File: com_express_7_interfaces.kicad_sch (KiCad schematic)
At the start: 1 part, among them J1 Plug_Bus_CE7_EPT_401-55501-51

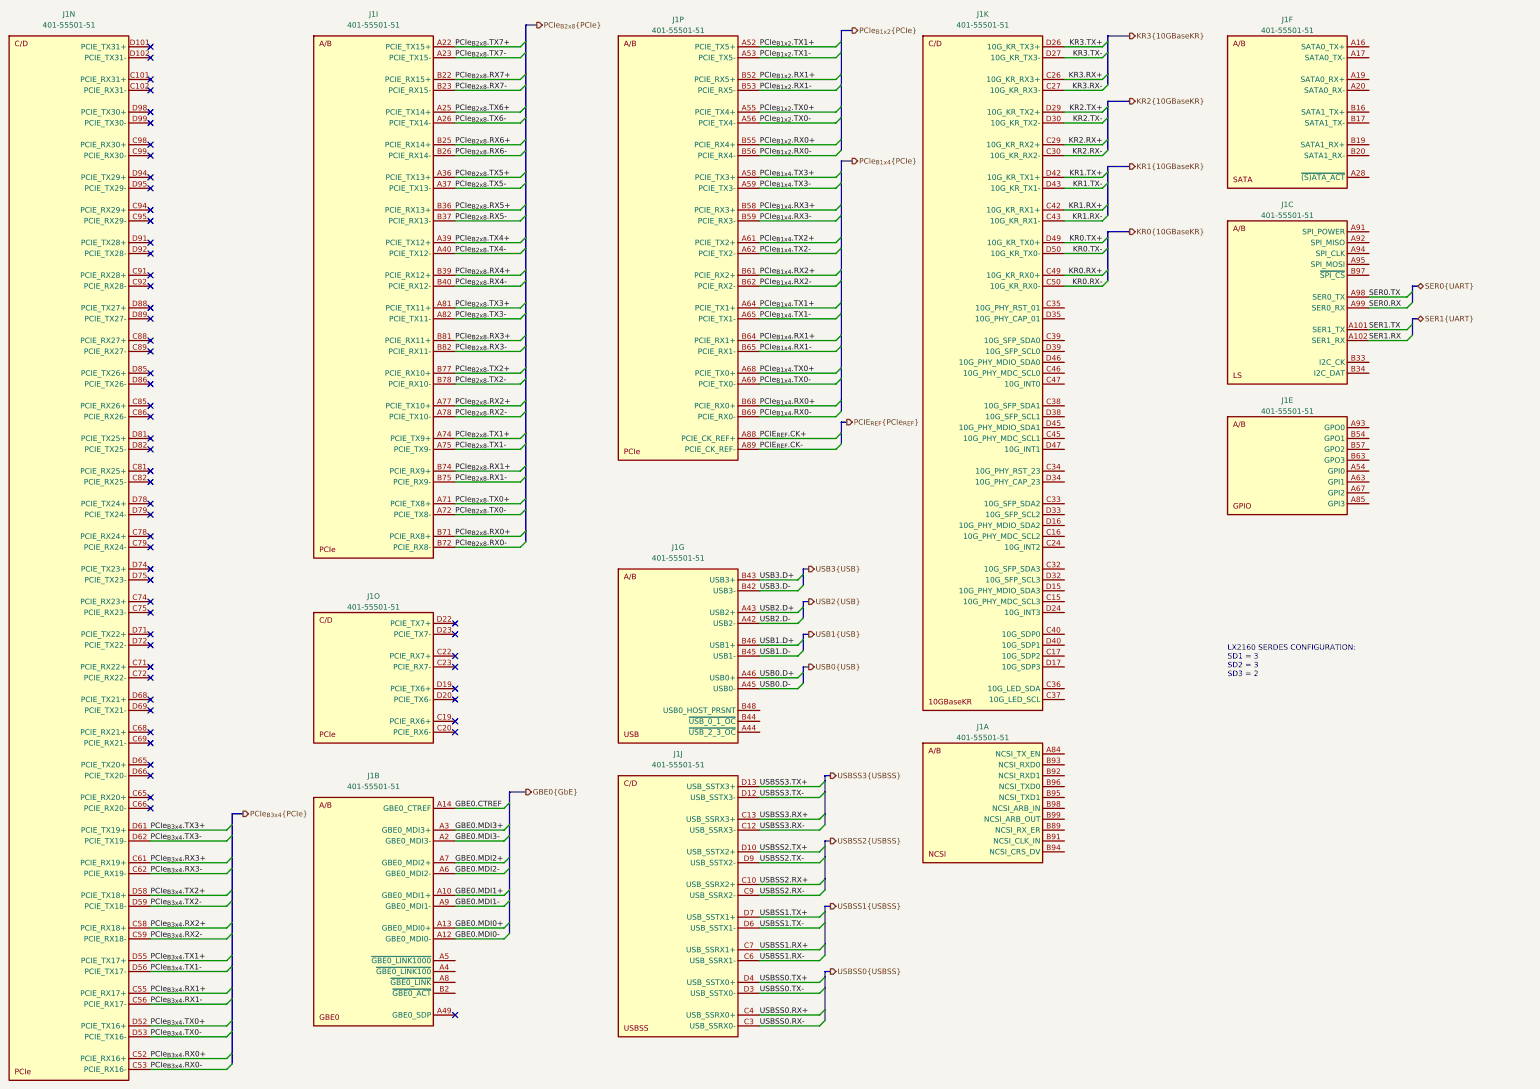
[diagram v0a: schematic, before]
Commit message: [#57056] Create schematics for M.2 and OCuLink connectors
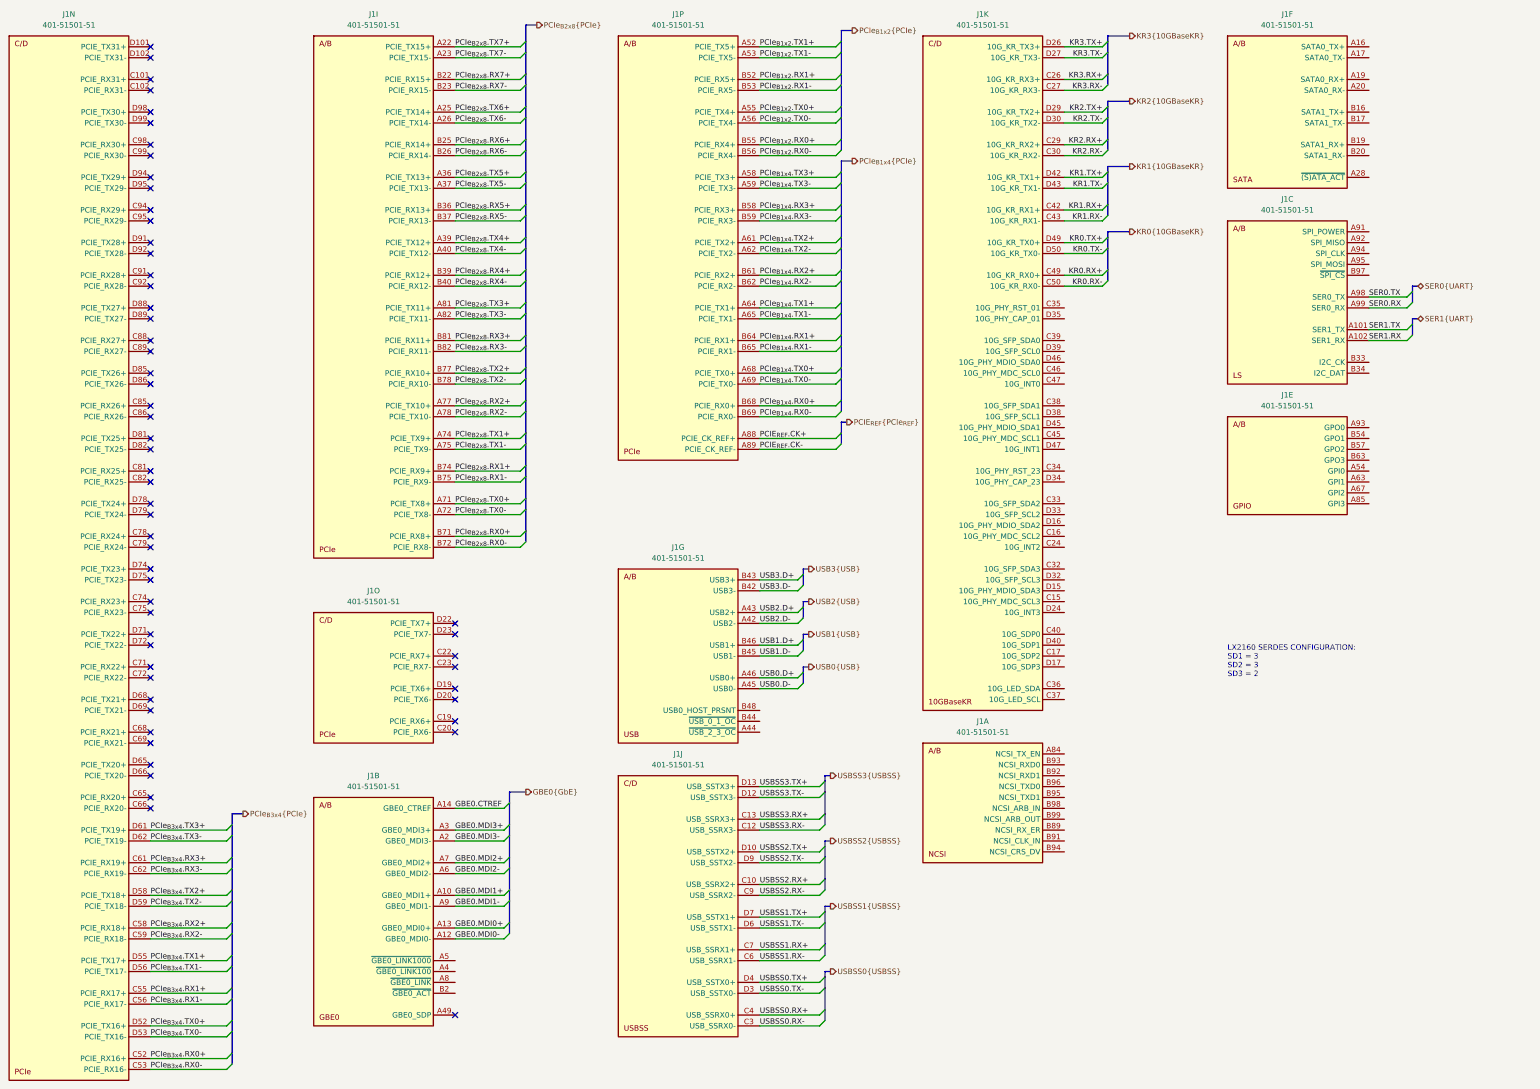
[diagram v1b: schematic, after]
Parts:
- J1: value Plug_Bus_CE7_EPT_401-55501-51 -> Plug_Bus_CE7_EPT_401-51501-51; footprint antmicro-footprints:EPT_401-55501-51 -> antmicro-footprints:EPT_401-51501-51; symbol antmicroB2BConnectors:Plug_Bus_CE7_EPT_401-55501-51 -> antmicroB2BConnectors:Plug_Bus_CE7_EPT_401-51501-51; MPN 401-55501-51 -> 401-51501-51

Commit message: [#57056] Connect GbE
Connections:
- net ~{GBE0_LINK_100}: now reaches J1.A4 (~{GBE0_LINK100})
- net ~{GBE0_LINK_1000}: now reaches J1.A5 (~{GBE0_LINK1000})
- net ~{GBE0_ACT}: now reaches J1.B2 (~{GBE0_ACT})
- no-connect marks 57 -> 58
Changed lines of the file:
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@@
   (no_connect (at 139.7 259.08))
   (no_connect (at 68.58 200.66))
+  (no_connect (at 139.7 251.46))
   (no_connect (at 68.58 81.28))
   (no_connect (at 68.58 43.18))
@@
     (stroke (width 0) (type default))
   )
+  (wire (pts (xy 148.59 246.38) (xy 139.7 246.38))
+    (stroke (width 0) (type default))
+  )
   (wire (pts (xy 68.58 233.68) (xy 86.36 233.68))
     (stroke (width 0) (type default))
@@
     (stroke (width 0) (type default))
   )
+  (wire (pts (xy 148.59 254) (xy 139.7 254))
+    (stroke (width 0) (type default))
+  )
   (wire (pts (xy 139.7 149.86) (xy 154.94 149.86))
     (stroke (width 0) (type default))
@@
   )
   (bus (pts (xy 229.87 85.09) (xy 229.87 80.01))
+    (stroke (width 0) (type default))
+  )
+  (wire (pts (xy 148.59 248.92) (xy 139.7 248.92))
     (stroke (width 0) (type default))
   )
@@
     (effects (font (size 1.27 1.27)) (justify left))
   )
+  (hierarchical_label "~{GBE0_ACT}" (shape output) (at 148.59 254 0) (fields_autoplaced)
+    (effects (font (size 1.27 1.27)) (justify left))
+  )
+  (hierarchical_label "~{GBE0_LINK_1000}" (shape output) (at 148.59 246.38 0) (fields_autoplaced)
+    (effects (font (size 1.27 1.27)) (justify left))
+  )
+  (hierarchical_label "~{GBE0_LINK_100}" (shape output) (at 148.59 248.92 0) (fields_autoplaced)
+    (effects (font (size 1.27 1.27)) (justify left))
+  )

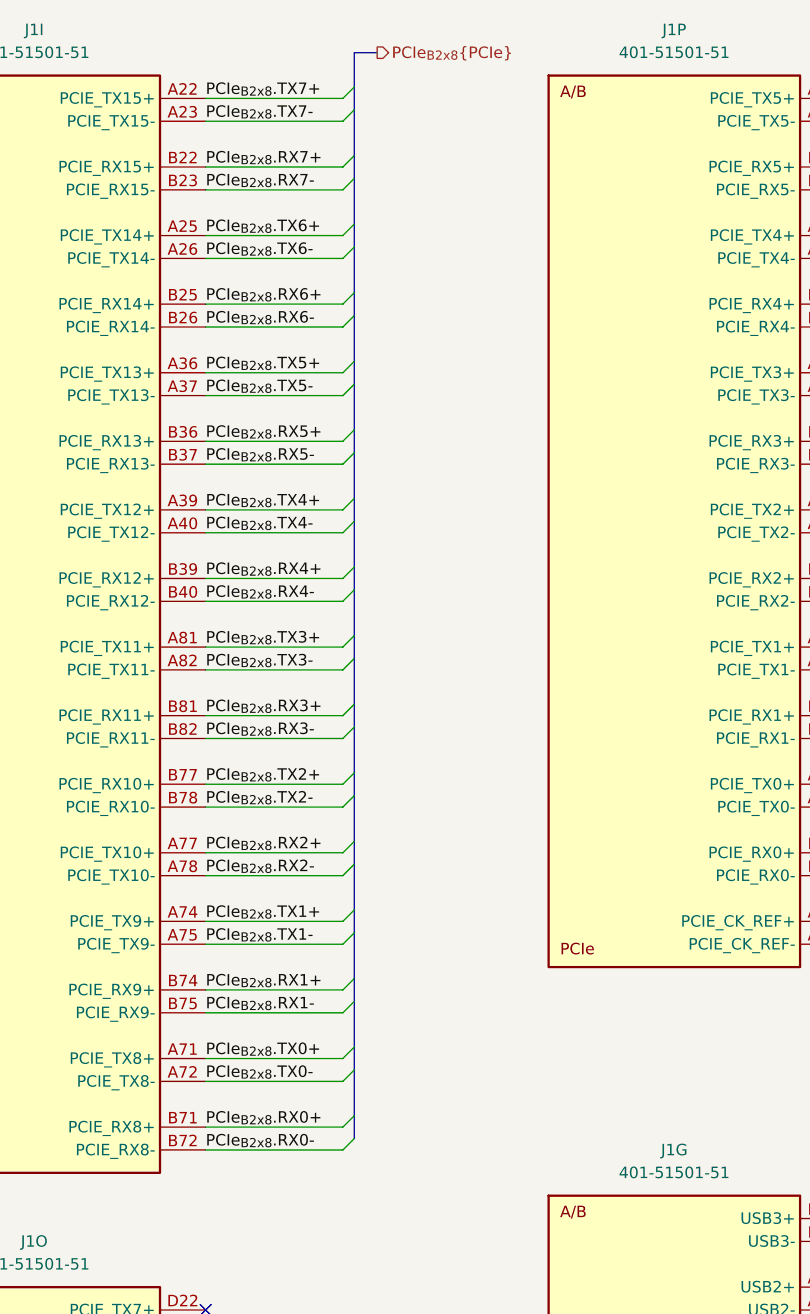
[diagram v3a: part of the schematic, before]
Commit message: [#57056] Update PCIe lane assignment, drop 2nd OCuLink
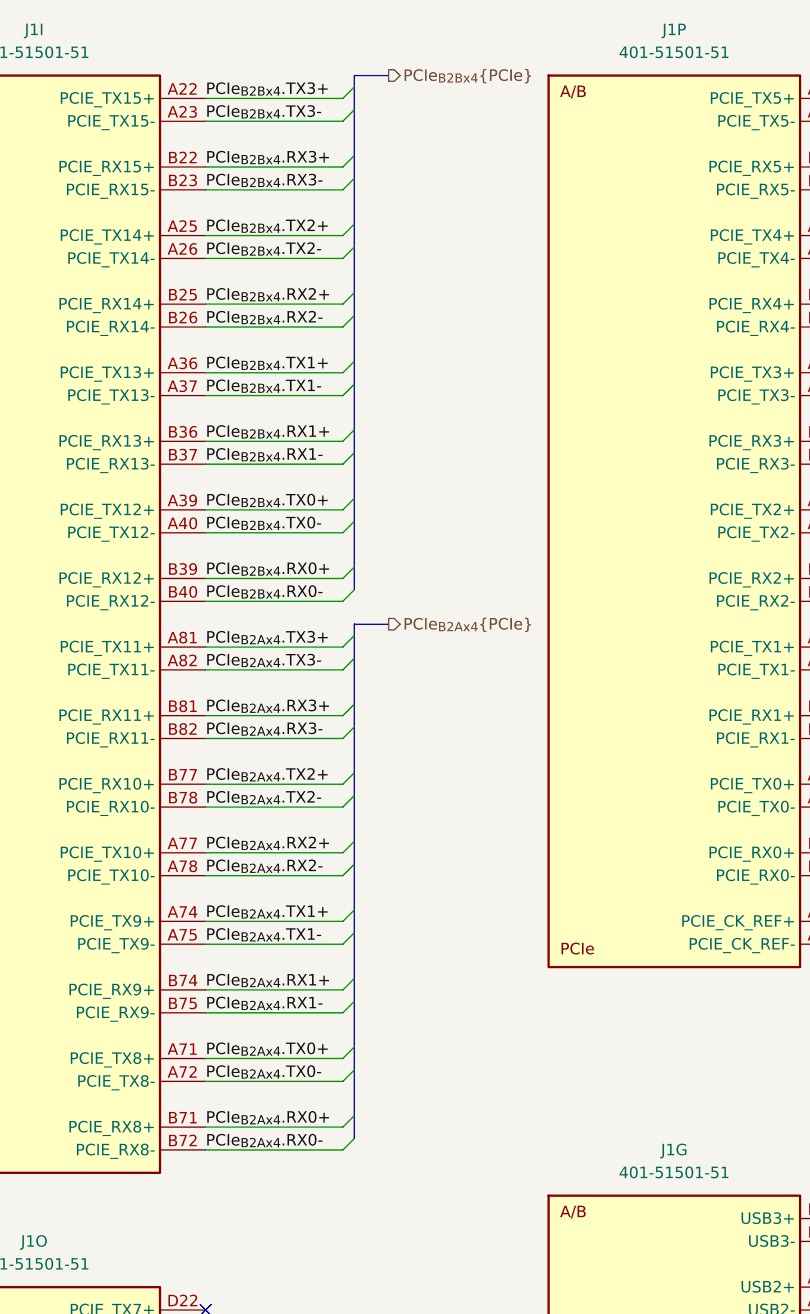
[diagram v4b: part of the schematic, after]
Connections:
- net PCIe_{B2x8}.RX0+ renamed PCIe_{B2Ax4}.RX0+
- net PCIe_{B2x8}.RX0- renamed PCIe_{B2Ax4}.RX0-
- net PCIe_{B2x8}.RX1+ renamed PCIe_{B2Ax4}.RX1+
- net PCIe_{B2x8}.RX1- renamed PCIe_{B2Ax4}.RX1-
- net PCIe_{B2x8}.RX2+ renamed PCIe_{B2Ax4}.RX2+
- net PCIe_{B2x8}.RX2- renamed PCIe_{B2Ax4}.RX2-
- net PCIe_{B2x8}.RX3+ renamed PCIe_{B2Ax4}.RX3+
- net PCIe_{B2x8}.RX3- renamed PCIe_{B2Ax4}.RX3-
- net PCIe_{B2x8}.RX4+ renamed PCIe_{B2Bx4}.RX0+
- net PCIe_{B2x8}.RX4- renamed PCIe_{B2Bx4}.RX0-
- net PCIe_{B2x8}.RX5+ renamed PCIe_{B2Bx4}.RX1+
- net PCIe_{B2x8}.RX5- renamed PCIe_{B2Bx4}.RX1-
- net PCIe_{B2x8}.RX6+ renamed PCIe_{B2Bx4}.RX2+
- net PCIe_{B2x8}.RX6- renamed PCIe_{B2Bx4}.RX2-
- net PCIe_{B2x8}.RX7+ renamed PCIe_{B2Bx4}.RX3+
- net PCIe_{B2x8}.RX7- renamed PCIe_{B2Bx4}.RX3-
- net PCIe_{B2x8}.TX0+ renamed PCIe_{B2Ax4}.TX0+
- net PCIe_{B2x8}.TX0- renamed PCIe_{B2Ax4}.TX0-
- net PCIe_{B2x8}.TX1+ renamed PCIe_{B2Ax4}.TX1+
- net PCIe_{B2x8}.TX1- renamed PCIe_{B2Ax4}.TX1-
- net PCIe_{B2x8}.TX2+ renamed PCIe_{B2Ax4}.TX2+
- net PCIe_{B2x8}.TX2- renamed PCIe_{B2Ax4}.TX2-
- net PCIe_{B2x8}.TX3+ renamed PCIe_{B2Ax4}.TX3+
- net PCIe_{B2x8}.TX3- renamed PCIe_{B2Ax4}.TX3-
- net PCIe_{B2x8}.TX4+ renamed PCIe_{B2Bx4}.TX0+
- net PCIe_{B2x8}.TX4- renamed PCIe_{B2Bx4}.TX0-
- net PCIe_{B2x8}.TX5+ renamed PCIe_{B2Bx4}.TX1+
- net PCIe_{B2x8}.TX5- renamed PCIe_{B2Bx4}.TX1-
- net PCIe_{B2x8}.TX6+ renamed PCIe_{B2Bx4}.TX2+
- net PCIe_{B2x8}.TX6- renamed PCIe_{B2Bx4}.TX2-
- net PCIe_{B2x8}.TX7+ renamed PCIe_{B2Bx4}.TX3+
- net PCIe_{B2x8}.TX7- renamed PCIe_{B2Bx4}.TX3-
